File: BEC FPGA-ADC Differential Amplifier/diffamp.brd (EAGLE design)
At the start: 53.6 x 34.6 mm, 23 parts, among them U1 ADA4807-2ARMZRM_8-M, X1 22-23-2031, X3 22-23-2021, X4 22-23-2021

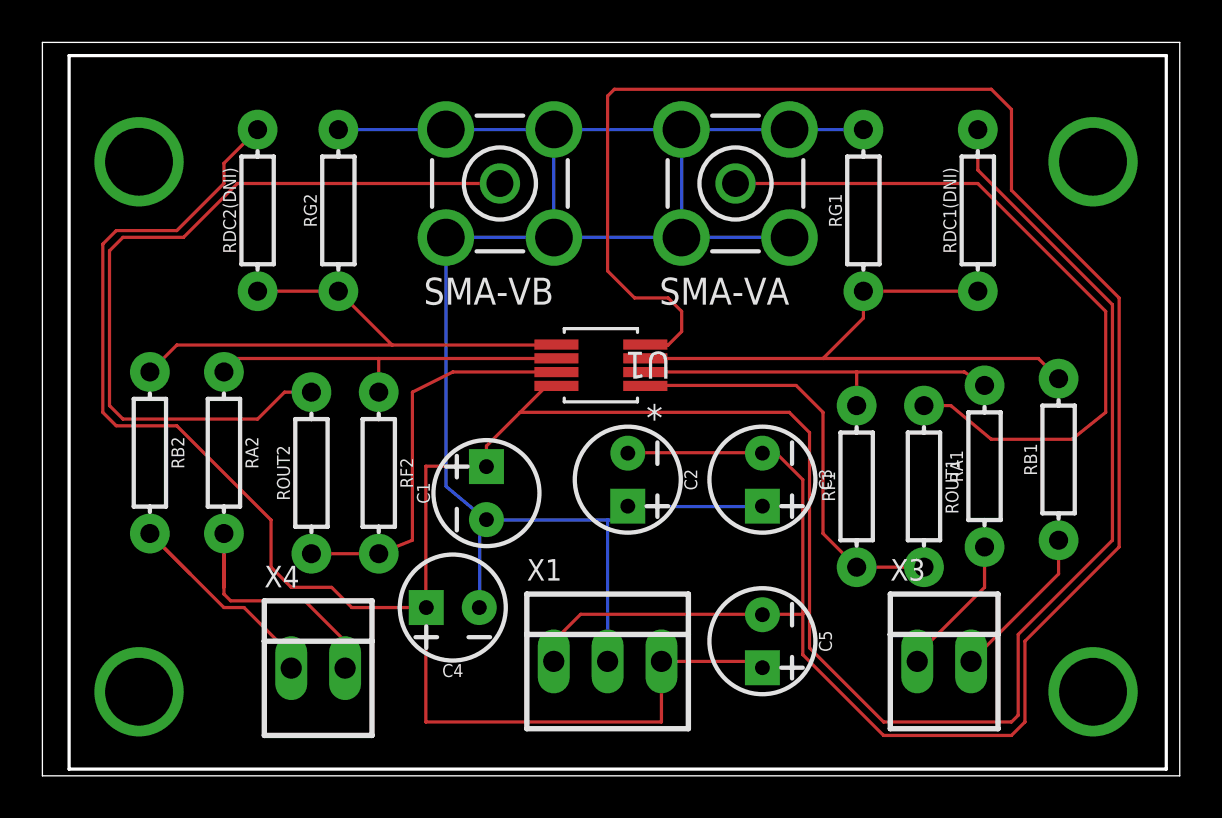
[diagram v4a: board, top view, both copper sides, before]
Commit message: Re-routed wires to leave more spacing on PCB.
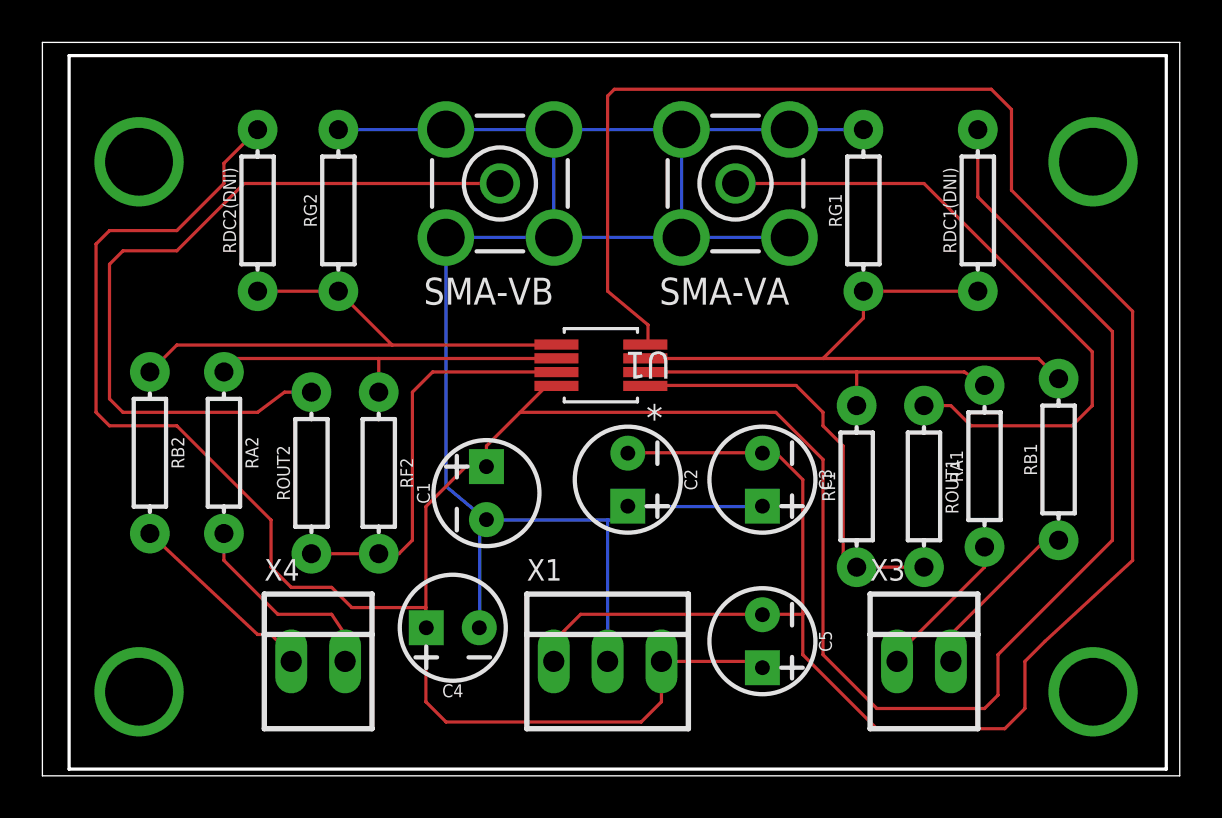
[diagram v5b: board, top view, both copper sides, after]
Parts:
- moved X3 0.95 mm to (73.0, 31.4)
- moved C4 0.95 mm to (50.8, 33.0)
- moved X4 0.32 mm to (44.5, 31.4)
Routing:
- net +5V: track 145.2 -> 141.4 mm
- net DAC-B1: track 13.3 -> 9.82 mm
- net DAC-B2: track 12.4 -> 9.26 mm
- net VSMA1: track 34.3 -> 31.4 mm
- net -5V: track 110.3 -> 107.6 mm
- net GND: track 91.8 -> 92.7 mm
- net VSMA2: track 37.3 -> 36.4 mm
- net DAC-A2: track 7.42 -> 8.19 mm
